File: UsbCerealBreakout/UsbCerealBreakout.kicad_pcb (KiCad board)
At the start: 2 copper layers, 23.5 x 18 mm, 3 parts, among them J1 Serial Connector, J2 USB_C_Data_Output, P1 USB_C_Plug

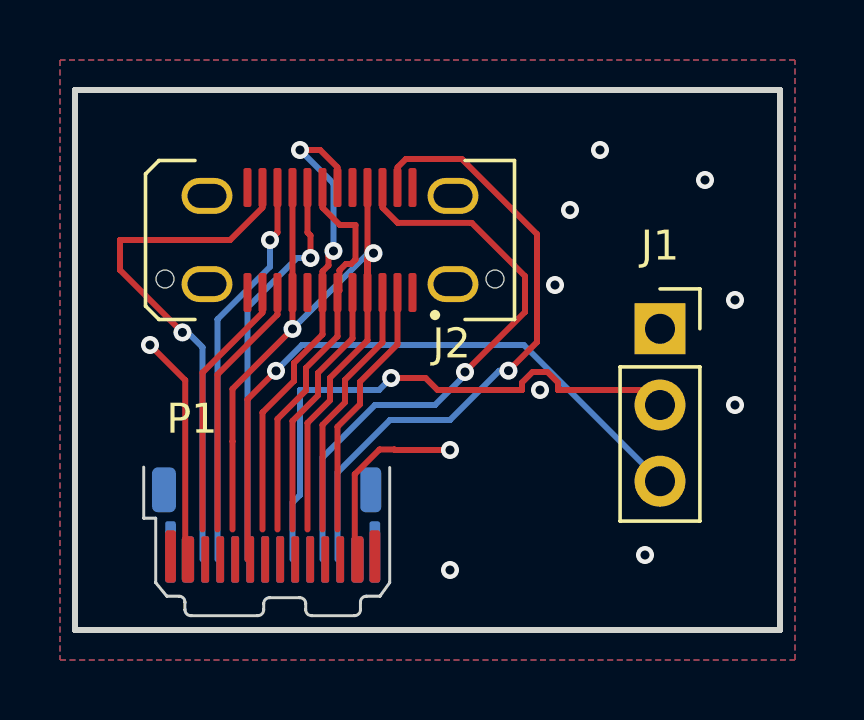
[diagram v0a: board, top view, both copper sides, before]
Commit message: Switch to Molex USB-C plug that is actually in stock
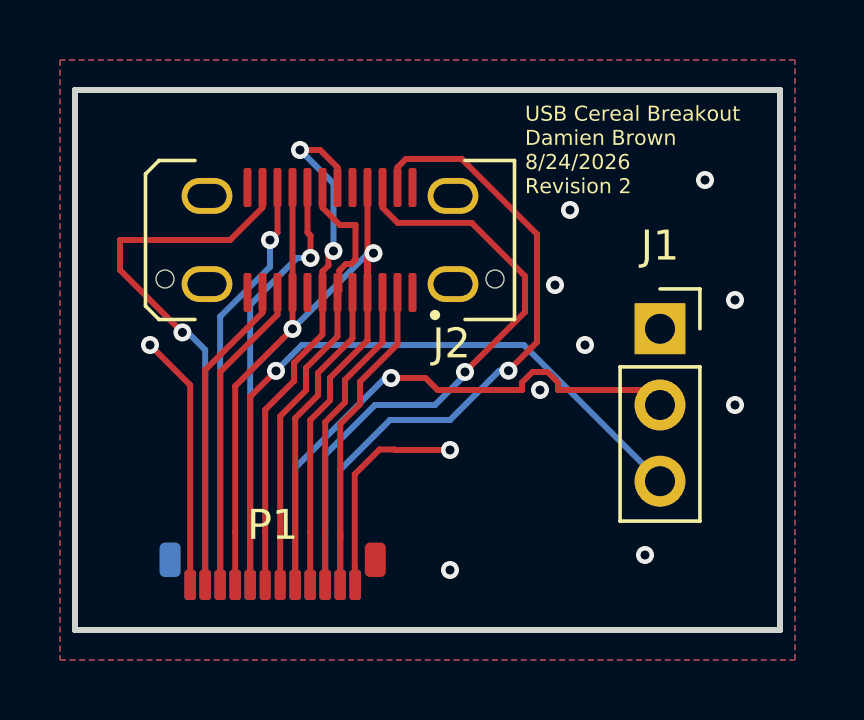
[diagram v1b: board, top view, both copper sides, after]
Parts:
- P1: footprint Connector_USB:USB_C_Plug_JAE_DX07P024AJ1 -> Connector_USB:USB_C_Plug_Molex_105444
- moved P1 2.04 mm to (129.1, 81.0), turned to 180 degrees
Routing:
- net Net-(J2-VBUS-PadA4): track 29.7 -> 33.3 mm
- net Net-(J2-TX1+): track 8.73 -> 10.8 mm
- net Net-(J2-TX1-): track 8.73 -> 10.5 mm
- net Net-(J2-CC1): track 8.73 -> 10.5 mm
- net Net-(P1-D-): track 16.2 -> 18.1 mm
- net Net-(P1-D+): track 13.8 -> 15.7 mm
- net Net-(J2-RX2-): track 8.73 -> 10.5 mm
- net Net-(J2-RX2+): track 8.73 -> 10.5 mm
- net GND: track 14.0 -> 15.8 mm
- net Net-(J2-TX2+): track 17.8 -> 18.6 mm
- net Net-(J2-CC2): track 13.6 -> 14.4 mm
- net Net-(J2-TX2-): track 13.2 -> 14.0 mm
- net Net-(J2-RX1-): track 19.8 -> 20.6 mm
- net Net-(J2-RX1+): track 21.4 -> 22.2 mm
- net Net-(J1-Pin_3): track 21.7 -> 22.5 mm
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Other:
- board text added: "USB Cereal Breakout Damien Brown 8/24/2026 Revision 2"
